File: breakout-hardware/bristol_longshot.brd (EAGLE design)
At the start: 67 parts, among them U1 SPV1040, U2 SPV1040, U3 L6924D, U4 TPS62243, U5 TPS62243, U6 TPS3808, U7 74LVC1G04GW

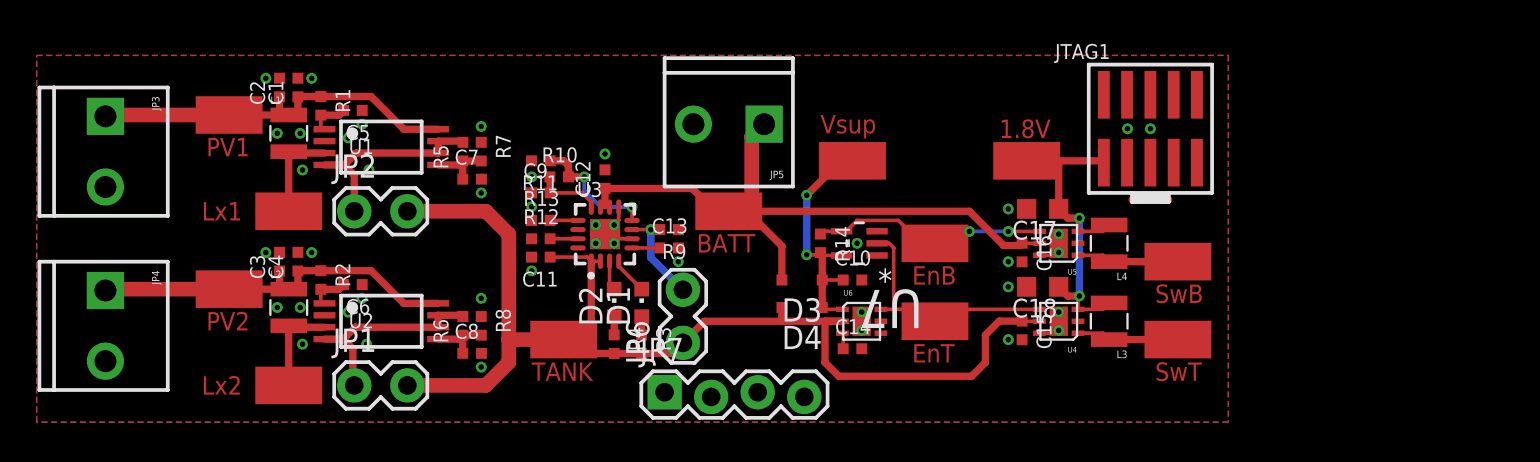
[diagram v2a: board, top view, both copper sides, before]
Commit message: Second revision. Modifications:
-Ref des inductors for mppt
-Pull-up on tank en
-Li-ion charger to LT4054
-Add TVS diods for mppt
-Capacitors both sides of jumpers
-More current in Vctrl divider. TODO partslist for this
-Fixed cream on supervisor
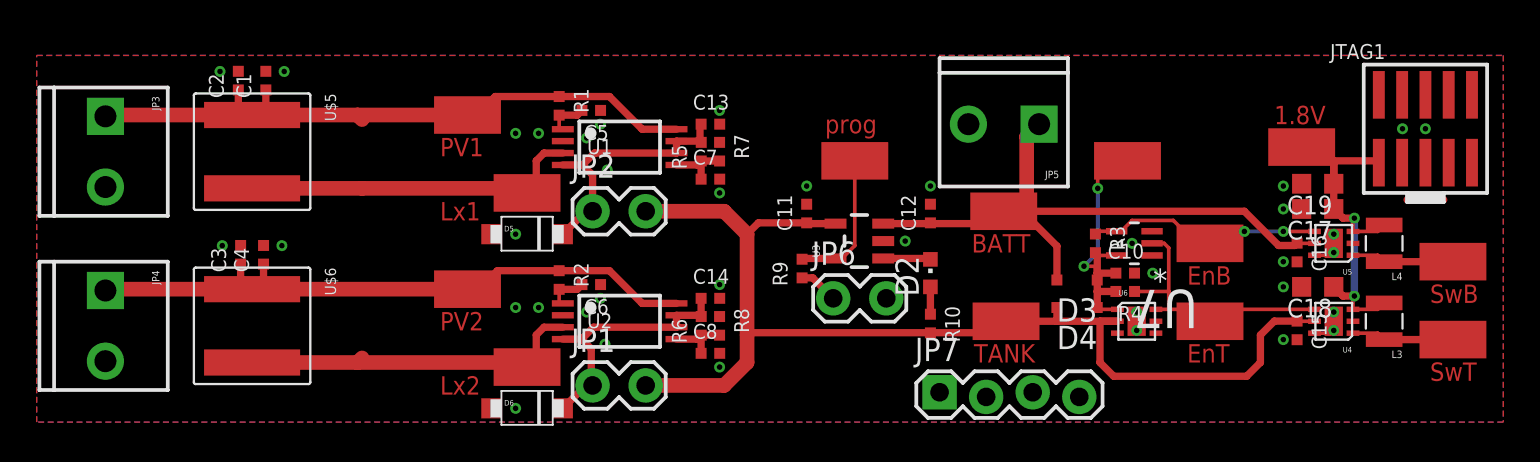
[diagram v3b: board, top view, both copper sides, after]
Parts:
- removed C9: 1nF, microbuilder_v3:_0402
- removed D1: GREEN, led:CHIPLED_0603
- removed L1, L2: 2.2µH, SparkFun:1007
- removed R11, R12: 47kΩ, microbuilder_v3:_0402
- removed R13, R14: 10kΩ, microbuilder_v3:_0402
- added C19: 10µF, resistor:C0603K
- added D5, D6: DIODE[TVS], nxp:SOD123W
- added U$25: S1751-46R, Harwin-Test-Point:S1751-46R
- added U$5, U$6: XAL6060, XAL6060:XAL60
- C13: value 47nF -> 4.7µF
- C14: value DNP -> 4.7µF
- R10: value 100kΩ -> 330Ω
- R3, R4: value 1kΩ -> 10kΩ
- R5, R6: value 2M2Ω -> 220kΩ
- R7, R8: value 820kΩ -> 82kΩ
- R9: value 100kΩ -> 2.2kΩ
- U3: value L6924D -> LT4054ES5-4.2; device l6924d:VFQFPN16 -> XYKlib:SOT23-5
- moved R4 28.0 mm to (59.4, 7.12), turned to 180 degrees
- moved R3 25.4 mm to (57.8, 9.75)
- moved U$41 24.1 mm to (52.9, 5.50)
- moved R10 21.8 mm to (48.8, 5.38), turned to 270 degrees
- moved C12 17.8 mm to (48.8, 11.4)
- moved D2 17.3 mm to (48.8, 8.12)
- moved U$42 15.0 mm to (69.0, 15.0)
- moved C15 15.0 mm to (68.8, 5.00)
- moved C16 15.0 mm to (68.8, 9.25)
- moved C17 15.0 mm to (69.9, 11.6)
- moved C18 15.0 mm to (69.9, 7.38)
- moved D3 15.0 mm to (56.8, 7.75)
- moved D4 15.0 mm to (56.8, 6.25)
- moved JP5 15.0 mm to (54.5, 16.2)
- moved JP7 15.0 mm to (49.2, 1.50)
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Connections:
- removed net IPRE: U3.P$16
- removed net N$2: C14.1, U6.3
- removed net N$3: C13.1, U3.P$5
- removed net N$6: D1.A, R3.1
- removed net N$8: D2.A, R4.1
- removed net REND: R13.2, U3.P$13
- removed net RPRG: R12.2, U3.P$15
- removed net SD: JP6.2, R9.2, U3.P$7
- removed net ST1: D1.C, U3.P$4
- removed net ST2: D2.C, U3.P$3
- removed net TH: R10.2, R11.1, U3.P$8
- removed net VPRE: U3.P$14
- removed net VREF: C9.2, R10.1, U3.P$12
- new net CHG: D2.C, U3.1
- new net CHG_LED: D2.A, R10.1
- new net CT: U6.3
- new net N$5: JP6.1, R9.1
- new net PROG: R9.2, U$25.PAD, U3.5
- net 1.8V: now also C19.1
- net BATTERY: now also U3.3; no longer U3.P$10, U3.P$11
- net BATTERY_EN: now also R3.1; no longer R14.1
- net GND: now also C19.2, D5.P$1, D6.P$1, JP6.2, U3.2; no longer C9.1, R11.2, R12.1, R13.1, R9.1, U3.P$17, U3.P$6, U3.P$9
- net LX1: now also U$5.P$2; no longer L1.2
- net LX2: now also U$6.P$2; no longer L2.2
- net MPPT-VOUT-1: now also C13.1, D5.P$2
- net MPPT-VOUT-2: now also C14.1, D6.P$2
- net PV1: now also U$5.P$1; no longer L1.1
- net PV2: now also U$6.P$1; no longer L2.1
- net SUPERVISOR_VCC: now also R3.2, R4.2; no longer R14.2
- net TANK: now also R10.2, U3.4; no longer JP6.1, R3.2, R4.2, U3.P$1, U3.P$2
- net TANK_EN: now also R4.1
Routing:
- net PV1: track 21.0 -> 36.3 mm
- net PV2: track 21.0 -> 35.5 mm
- net LX2: track 5.20 -> 19.0 mm
- net LX1: track 5.23 -> 18.7 mm
- net PROG: track 0.00 -> 7.81 mm
- net TH: track 7.04 -> 0.00 mm, vias 2 -> 0
- net SD: track 5.52 -> 0.00 mm, vias 1 -> 0
- net GND: track 6.76 -> 2.40 mm, vias 42 -> 38
- net VREF: track 3.60 -> 0.00 mm
- net MPPT-VOUT-2: track 11.3 -> 14.4 mm
- net MPPT-VOUT-1: track 11.2 -> 14.3 mm
- net BATTERY: track 37.4 -> 34.6 mm
- net CHG: track 0.00 -> 2.60 mm
- net SUPERVISOR_VCC: track 13.9 -> 16.1 mm
- net N$5: track 0.00 -> 2.16 mm
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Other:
- board text added: "prog"
- board text removed: "Vsup"
